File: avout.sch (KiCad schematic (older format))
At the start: 53 parts, among them CN6 AUDIO_VIDEO, M1 Modulator, Q3 2SC1815, Q81 2SC1815, Q82 2SC1815

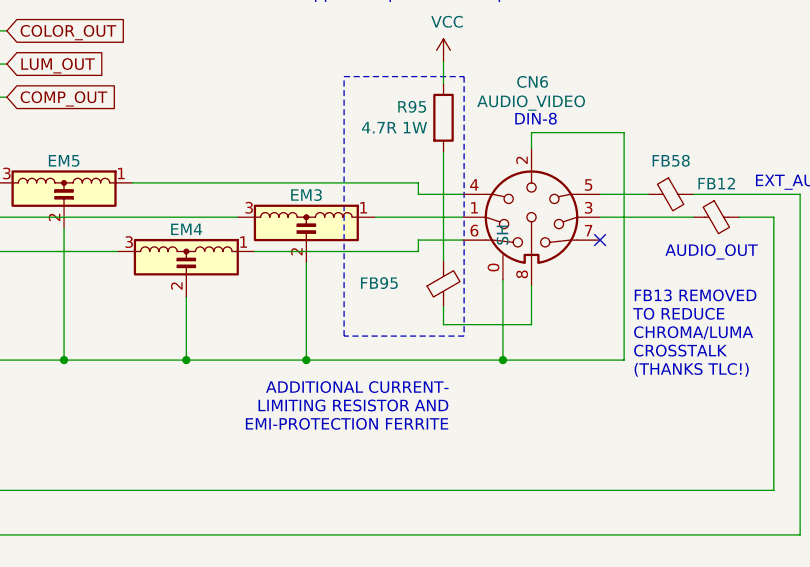
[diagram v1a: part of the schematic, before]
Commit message: Add ROM bank switcher (All-in-one ROM only)
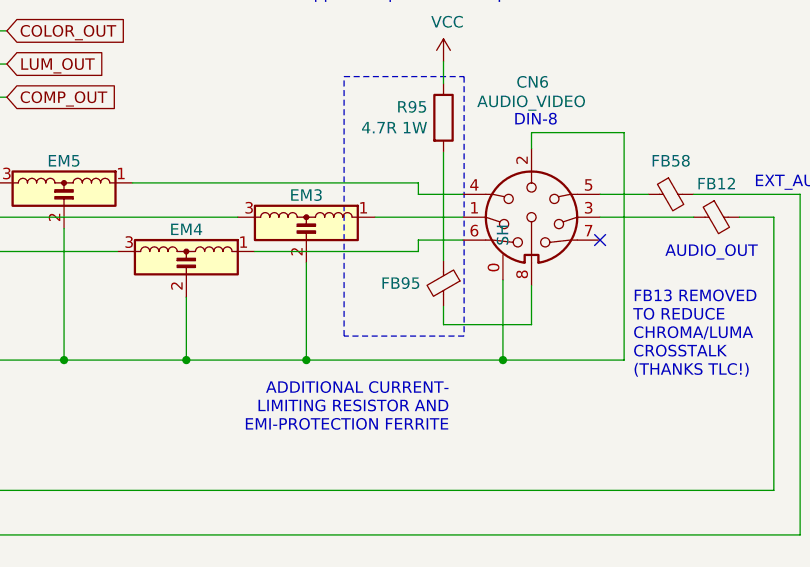
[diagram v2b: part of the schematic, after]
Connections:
- net at R95.2: now also FB95.1; no longer FB95.2
- net at CN6.8: now also FB95.2; no longer FB95.1
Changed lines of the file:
@@
 U 1 1 61E4B6DF
 P 9260 2605
-F 0 "FB95" H 9066 2605 50  0000 R CNN
+F 0 "FB95" H 9360 2605 50  0000 L CNN
 F 1 "Ferrite_Bead_Small" H 9360 2560 50  0001 L CNN
 F 2 "LittleSixteen:Ferrite" V 9190 2605 50  0001 C CNN
 F 3 "~" H 9260 2605 50  0001 C CNN
 	1    9260 2605
-	1    0    0    1
+	-1   0    0    -1
 $EndComp
 Wire Wire Line

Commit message: Rationalize BOM There should be no significant changes on both schematics on PCB, just some values and something on the silkscreen
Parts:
- removed EM3, EM4, EM5: EMI_Filter_LCL, LittleSixteen:EMI_Filter, symbol Device:EMI_Filter_LCL
- added EM3, EM4, EM5: DSS1NB32A271Q91A, LittleSixteen:EMI_Filter, symbol emi_filter_3pin:EMI_Filter_3Pin
- C11, C85: MouserPN (none) -> 810-FG28X7R1H104KNT0
- C83: value 100u/25V -> 100u/35V
- C84: MouserPN (none) -> 810-FG28C0G2A101JNT6
- FB12, FB58, FB95: value Ferrite_Bead_Small -> DSS1NB32A271Q91A; footprint LittleSixteen:Ferrite -> LittleSixteen:EMI_Filter; symbol ferrite_bead_small:Ferrite_Bead_Small -> emi_filter_3pin:EMI_Filter_3Pin
- JP81: value RV1_BYPASS -> JMP_RV1_BYPASS
- JP82: value RV2_BYPASS -> JMP_RV2_BYPASS
- L80, L81: value 10u -> FERRITE; MouserPN (none) -> 875-28C0236-0EW-10
- R95: value 4.7R 1W -> 4.7 1W
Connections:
- net COLOR_OUT: now also EM4.2
- net COMP_OUT: now also EM5.2
- net GND: now also EM3.3 (GND), EM4.3 (GND), EM5.3 (GND)
- net LUM_OUT: now also EM3.2
- net VCC: now also R95.2; no longer R95.1
- net at CN6.4: now also EM5.1
- net at CN6.1: now also EM3.1
- net at CN6.6: now also EM4.1
- net at FB95.1: now also R95.1; no longer R95.2
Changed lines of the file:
@@
 F 2 "Capacitor_THT:C_Disc_D8.0mm_W2.5mm_P5.00mm" H 1033 5430 50  0001 C CNN
 F 3 "~" H 995 5580 50  0001 C CNN
+F 4 "810-FG28X7R1H104KNT0" H 995 5580 50  0001 C CNN "MouserPN"
 	1    995  5580
 	1    0    0    -1
@@
 	1    0    0    -1
 $EndComp
-$Comp
-L Device:EMI_Filter_LCL EM5
-U 1 1 5E029075
-P 7600 2265
-F 0 "EM5" H 7600 2460 50  0000 C CNN
-F 1 "EMI_Filter_LCL" H 7600 2491 50  0001 C CNN
-F 2 "LittleSixteen:EMI_Filter" V 7600 2265 50  0001 C CNN
-F 3 "http://www.murata.com/~/media/webrenewal/support/library/catalog/products/emc/emifil/c31e.ashx?la=en-gb" V 7600 2265 50  0001 C CNN
-	1    7600 2265
-	-1   0    0    -1
-$EndComp
-$Comp
-L Device:EMI_Filter_LCL EM3
-U 1 1 5E02CB2E
-P 8660 2415
-F 0 "EM3" H 8660 2610 50  0000 C CNN
-F 1 "EMI_Filter_LCL" H 8660 2641 50  0001 C CNN
-F 2 "LittleSixteen:EMI_Filter" V 8660 2415 50  0001 C CNN
-F 3 "http://www.murata.com/~/media/webrenewal/support/library/catalog/products/emc/emifil/c31e.ashx?la=en-gb" V 8660 2415 50  0001 C CNN
-	1    8660 2415
-	-1   0    0    -1
-$EndComp
-$Comp
-L Device:EMI_Filter_LCL EM4
-U 1 1 5E02E767
-P 8135 2565
-F 0 "EM4" H 8135 2760 50  0000 C CNN
-F 1 "EMI_Filter_LCL" H 8135 2791 50  0001 C CNN
-F 2 "LittleSixteen:EMI_Filter" V 8135 2565 50  0001 C CNN
-F 3 "http://www.murata.com/~/media/webrenewal/support/library/catalog/products/emc/emifil/c31e.ashx?la=en-gb" V 8135 2565 50  0001 C CNN
-	1    8135 2565
-	-1   0    0    -1
-$EndComp
 Wire Wire Line
 	6660 2165 7210 2165
@@
 	6660 2315 7125 2315
 Wire Wire Line
-	8960 2315 9345 2315
-Wire Wire Line
-	8435 2465 9150 2465
-Wire Wire Line
-	9150 2465 9150 2415
-Wire Wire Line
 	9150 2415 9345 2415
 Wire Wire Line
@@
 Wire Wire Line
 	9150 2215 9345 2215
-Wire Wire Line
-	7900 2165 9150 2165
-Wire Wire Line
-	7600 2365 7600 2940
-Wire Wire Line
-	8135 2665 8135 2940
-Wire Wire Line
-	8135 2940 7600 2940
-Connection ~ 7600 2940
-Wire Wire Line
-	8660 2515 8660 2940
-Wire Wire Line
-	8660 2940 8135 2940
-Connection ~ 8135 2940
 Text Notes 9760 1925 2    50   ~ 0
 DIN-8
@@
 Wire Wire Line
 	10050 2940 9520 2940
-Connection ~ 8660 2940
 Wire Wire Line
 	9645 2615 9645 2785
@@
 $EndComp
 $Comp
-L ferrite_bead_small:Ferrite_Bead_Small FB12
+L emi_filter_3pin:EMI_Filter_3Pin FB12
 U 1 1 5E03F938
 P 10455 2315
 F 0 "FB12" V 10310 2315 50  0000 C CNN
-F 1 "Ferrite_Bead_Small" H 10555 2270 50  0001 L CNN
-F 2 "LittleSixteen:Ferrite" V 10385 2315 50  0001 C CNN
+F 1 "DSS1NB32A271Q91A" H 10555 2270 50  0001 L CNN
+F 2 "LittleSixteen:EMI_Filter" V 10385 2315 50  0001 C CNN
 F 3 "~" H 10455 2315 50  0001 C CNN
 	1    10455 2315
@@
 $EndComp
 $Comp
-L ferrite_bead_small:Ferrite_Bead_Small FB58
+L emi_filter_3pin:EMI_Filter_3Pin FB58
 U 1 1 5E040A9B
 P 10255 2215
 F 0 "FB58" V 10110 2215 50  0000 C CNN
-F 1 "Ferrite_Bead_Small" H 10355 2170 50  0001 L CNN
-F 2 "LittleSixteen:Ferrite" V 10185 2215 50  0001 C CNN
+F 1 "DSS1NB32A271Q91A" H 10355 2170 50  0001 L CNN
+F 2 "LittleSixteen:EMI_Filter" V 10185 2215 50  0001 C CNN
 F 3 "~" H 10255 2215 50  0001 C CNN
 	1    10255 2215
@@
 P 4805 6860
 F 0 "L81" V 4995 6860 50  0000 C CNN
-F 1 "10u" V 4904 6860 50  0000 C CNN
+F 1 "FERRITE" V 4904 6860 50  0000 C CNN
 F 2 "Inductor_THT:L_Axial_L7.0mm_D3.3mm_P12.70mm_Horizontal_Fastron_MICC" H 4805 6860 50  0001 C CNN
 F 3 "~" H 4805 6860 50  0001 C CNN
+F 4 "875-28C0236-0EW-10" H 4805 6860 50  0001 C CNN "MouserPN"
 	1    4805 6860
 	0    -1   -1   0
@@
 P 1260 5580
 F 0 "C83" H 1145 5626 50  0000 R CNN
-F 1 "100u/25V" H 1145 5535 50  0000 R CNN
+F 1 "100u/35V" H 1145 5535 50  0000 R CNN
 F 2 "Capacitor_THT:CP_Radial_D6.3mm_P2.50mm" H 1260 5580 50  0001 C CNN
 F 3 "~" H 1260 5580 50  0001 C CNN
@@
 Connection ~ 7040 2465
 Wire Wire Line
-	7040 2465 7835 2465
-Wire Wire Line
 	7125 2315 7125 1645
 Wire Wire Line
@@
 Connection ~ 7125 2315
 Wire Wire Line
-	7125 2315 8360 2315
-Wire Wire Line
 	7210 2165 7210 1790
 Wire Wire Line
 	7210 1790 7350 1790
 Connection ~ 7210 2165
-Wire Wire Line
-	7210 2165 7300 2165
 Text GLabel 7350 1790 2    50   Input ~ 0
 COMP_OUT
@@
 	9520 2590 9520 2940
 Connection ~ 9520 2940
-Wire Wire Line
-	9520 2940 8660 2940
 $Comp
 L Device:R R?
@@
 AR Path="/61BCD018/61DEF839" Ref="R?"  Part="1"
 AR Path="/5E019FCB/61DEF839" Ref="R95"  Part="1"
-F 0 "R95" H 9190 1926 50  0000 R CNN
-F 1 "4.7R 1W" H 9190 1835 50  0000 R CNN
+F 0 "R95" H 9330 1834 50  0000 L CNN
+F 1 "4.7 1W" H 9330 1925 50  0000 L CNN
 F 2 "Resistor_THT:R_Axial_DIN0414_L11.9mm_D4.5mm_P5.08mm_Vertical" V 9190 1880 50  0001 C CNN
 F 3 "~" H 9260 1880 50  0001 C CNN
 	1    9260 1880
-	1    0    0    -1
+	-1   0    0    1
 $EndComp
 Wire Wire Line
 	9260 1730 9260 1635
 $Comp
-L ferrite_bead_small:Ferrite_Bead_Small FB95
+L emi_filter_3pin:EMI_Filter_3Pin FB95
 U 1 1 61E4B6DF
 P 9260 2605
 F 0 "FB95" H 9360 2605 50  0000 L CNN
-F 1 "Ferrite_Bead_Small" H 9360 2560 50  0001 L CNN
-F 2 "LittleSixteen:Ferrite" V 9190 2605 50  0001 C CNN
+F 1 "DSS1NB32A271Q91A" H 9360 2560 50  0001 L CNN
+F 2 "LittleSixteen:EMI_Filter" V 9190 2605 50  0001 C CNN
 F 3 "~" H 9260 2605 50  0001 C CNN
 	1    9260 2605
@@
 P 3985 7345
 F 0 "L80" V 4175 7345 50  0000 C CNN
-F 1 "10u" V 4084 7345 50  0000 C CNN
+F 1 "FERRITE" V 4084 7345 50  0000 C CNN
 F 2 "Inductor_THT:L_Radial_D6.0mm_P4.00mm" H 3985 7345 50  0001 C CNN
 F 3 "~" H 3985 7345 50  0001 C CNN
+F 4 "875-28C0236-0EW-10" H 3985 7345 50  0001 C CNN "MouserPN"
 	1    3985 7345
 	0    -1   -1   0
@@
 Wire Wire Line
 	1130 5775 1260 5775
-Wire Wire Line
-	6480 2940 7600 2940
 $Comp
 L power:VCC #PWR0178
@@
 F 2 "Capacitor_THT:C_Disc_D8.0mm_W2.5mm_P5.00mm" H 3833 4555 50  0001 C CNN
 F 3 "~" H 3795 4705 50  0001 C CNN
+F 4 "810-FG28X7R1H104KNT0" H 3795 4705 50  0001 C CNN "MouserPN"
 	1    3795 4705
 	0    -1   -1   0
@@
 P 4835 5175
 F 0 "JP81" H 4835 5387 50  0000 C CNN
-F 1 "RV1_BYPASS" H 4835 5296 50  0000 C CNN
+F 1 "JMP_RV1_BYPASS" H 4835 5296 50  0000 C CNN
 F 2 "Jumper:SolderJumper-2_P1.3mm_Bridged_RoundedPad1.0x1.5mm" H 4835 5175 50  0001 C CNN
 F 3 "~" H 4835 5175 50  0001 C CNN
@@
 P 9215 5420
 F 0 "JP82" H 9215 5632 50  0000 C CNN
-F 1 "RV2_BYPASS" H 9215 5541 50  0000 C CNN
+F 1 "JMP_RV2_BYPASS" H 9215 5541 50  0000 C CNN
 F 2 "Jumper:SolderJumper-2_P1.3mm_Bridged_RoundedPad1.0x1.5mm" H 9215 5420 50  0001 C CNN
 F 3 "~" H 9215 5420 50  0001 C CNN
@@
 F 2 "Capacitor_THT:C_Disc_D8.0mm_W2.5mm_P5.00mm" H 2758 5250 50  0001 C CNN
 F 3 "~" H 2720 5400 50  0001 C CNN
+F 4 "810-FG28C0G2A101JNT6" H 2720 5400 50  0001 C CNN "MouserPN"
 	1    2720 5400
 	-1   0    0    1
@@
 Text Notes 10090 3020 0    50   ~ 0
 FB13 REMOVED\nTO REDUCE\nCHROMA/LUMA\nCROSSTALK\n(THANKS TLC!)
+Wire Wire Line
+	6480 2940 9520 2940
+Wire Wire Line
+	7210 2165 7475 2165
+Wire Wire Line
+	7675 2165 9150 2165
+$Comp
+L emi_filter_3pin:EMI_Filter_3Pin EM5
+U 1 1 67130B45
+P 7575 2165
+F 0 "EM5" V 7720 2165 50  0000 C CNN
+F 1 "DSS1NB32A271Q91A" H 7675 2120 50  0001 L CNN
+F 2 "LittleSixteen:EMI_Filter" V 7505 2165 50  0001 C CNN
+F 3 "~" H 7575 2165 50  0001 C CNN
+	1    7575 2165
+	0    1    -1   0
+$EndComp
+$Comp
+L emi_filter_3pin:EMI_Filter_3Pin EM4
+U 1 1 6714E1C3
+P 8145 2465
+F 0 "EM4" V 8000 2465 50  0000 C CNN
+F 1 "DSS1NB32A271Q91A" H 8245 2420 50  0001 L CNN
+F 2 "LittleSixteen:EMI_Filter" V 8075 2465 50  0001 C CNN
+F 3 "~" H 8145 2465 50  0001 C CNN
+	1    8145 2465
+	0    1    -1   0
+$EndComp
+Wire Wire Line
+	7040 2465 8045 2465
+$Comp
+L emi_filter_3pin:EMI_Filter_3Pin EM3
+U 1 1 6716F690
+P 8620 2315
+F 0 "EM3" V 8475 2315 50  0000 C CNN
+F 1 "DSS1NB32A271Q91A" H 8720 2270 50  0001 L CNN
+F 2 "LittleSixteen:EMI_Filter" V 8550 2315 50  0001 C CNN
+F 3 "~" H 8620 2315 50  0001 C CNN
+	1    8620 2315
+	0    1    -1   0
+$EndComp
+Wire Wire Line
+	7125 2315 8520 2315
+Wire Wire Line
+	8720 2315 9345 2315
+Wire Wire Line
+	9150 2495 8360 2495
+Wire Wire Line
+	8360 2495 8360 2465
+Wire Wire Line
+	8360 2465 8245 2465
+Wire Wire Line
+	9150 2415 9150 2495
 $EndSCHEMATC

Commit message: Rationalize capacitor footprints & BOM
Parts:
- C18, C19, C62: footprint Capacitor_THT:CP_Radial_D5.0mm_P2.50mm -> Capacitor_THT:CP_Radial_D5.0mm_P2.00mm; MouserPN (none) -> 710-860010672009
- C31: footprint Capacitor_THT:CP_Radial_D6.3mm_P2.50mm -> Capacitor_THT:CP_Radial_D5.0mm_P2.00mm; MouserPN (none) -> 710-860010672009
- JP81, JP82: MouserPN (none) -> ---
- L1: value 1.2u -> FERRITE; MouserPN (none) -> 875-28C0236-0EW-10
- L81: value FERRITE -> 10u; MouserPN 875-28C0236-0EW-10 -> 542-78F100-RC
- R11, R25: MouserPN (none) -> 603-MFR-25FBF52-100K
- R23: MouserPN (none) -> 603-MFR-25FTF52-10K
- R24, R28, R43, R8, R82: MouserPN (none) -> 603-MFR-25FBF52-1K
- R85: MouserPN (none) -> 708-RNF14FTD100R
- RV1: MouserPN (none) -> 652-3296W-1-102LF
- RV2: MouserPN (none) -> 652-3296W-1-221LF
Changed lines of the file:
@@
 P 6010 1220
 F 0 "L1" H 6062 1266 50  0000 L CNN
-F 1 "1.2u" H 6062 1175 50  0000 L CNN
+F 1 "FERRITE" H 6062 1175 50  0000 L CNN
 F 2 "Inductor_THT:L_Radial_D6.0mm_P4.00mm" H 6010 1220 50  0001 C CNN
 F 3 "~" H 6010 1220 50  0001 C CNN
+F 4 "875-28C0236-0EW-10" H 6010 1220 50  0001 C CNN "MouserPN"
 	1    6010 1220
 	1    0    0    -1
@@
 F 2 "Resistor_THT:R_Axial_DIN0207_L6.3mm_D2.5mm_P5.08mm_Vertical" V 1655 1965 50  0001 C CNN
 F 3 "~" H 1725 1965 50  0001 C CNN
+F 4 "603-MFR-25FBF52-1K" H 1725 1965 50  0001 C CNN "MouserPN"
 	1    1725 1965
 	0    -1   -1   0
@@
 F 2 "Resistor_THT:R_Axial_DIN0207_L6.3mm_D2.5mm_P5.08mm_Vertical" V 1380 2185 50  0001 C CNN
 F 3 "~" H 1450 2185 50  0001 C CNN
+F 4 "603-MFR-25FBF52-100K" H 1450 2185 50  0001 C CNN "MouserPN"
 	1    1450 2185
 	-1   0    0    1
@@
 F 0 "C18" V 1893 1965 50  0000 C CNN
 F 1 "10u/25V" V 1984 1965 50  0000 C CNN
-F 2 "Capacitor_THT:CP_Radial_D5.0mm_P2.50mm" H 2145 1965 50  0001 C CNN
+F 2 "Capacitor_THT:CP_Radial_D5.0mm_P2.00mm" H 2145 1965 50  0001 C CNN
 F 3 "~" H 2145 1965 50  0001 C CNN
+F 4 "710-860010672009" H 2145 1965 50  0001 C CNN "MouserPN"
 	1    2145 1965
 	0    1    1    0
@@
 F 2 "Resistor_THT:R_Axial_DIN0207_L6.3mm_D2.5mm_P5.08mm_Vertical" V 3385 1700 50  0001 C CNN
 F 3 "~" H 3455 1700 50  0001 C CNN
+F 4 "603-MFR-25FBF52-1K" H 3455 1700 50  0001 C CNN "MouserPN"
 	1    3455 1700
 	0    -1   -1   0
@@
 F 2 "Resistor_THT:R_Axial_DIN0207_L6.3mm_D2.5mm_P5.08mm_Vertical" V 3020 1385 50  0001 C CNN
 F 3 "~" H 3090 1385 50  0001 C CNN
+F 4 "603-MFR-25FTF52-10K" H 3090 1385 50  0001 C CNN "MouserPN"
 	1    3090 1385
 	-1   0    0    1
@@
 F 0 "C31" V 4708 2935 50  0000 C CNN
 F 1 "10u/25V" V 4799 2935 50  0000 C CNN
-F 2 "Capacitor_THT:CP_Radial_D6.3mm_P2.50mm" H 4960 2935 50  0001 C CNN
+F 2 "Capacitor_THT:CP_Radial_D5.0mm_P2.00mm" H 4960 2935 50  0001 C CNN
 F 3 "~" H 4960 2935 50  0001 C CNN
+F 4 "710-860010672009" H 4960 2935 50  0001 C CNN "MouserPN"
 	1    4960 2935
 	0    -1   1    0
@@
 F 2 "Resistor_THT:R_Axial_DIN0207_L6.3mm_D2.5mm_P5.08mm_Vertical" V 5220 3165 50  0001 C CNN
 F 3 "~" H 5290 3165 50  0001 C CNN
+F 4 "603-MFR-25FBF52-100K" H 5290 3165 50  0001 C CNN "MouserPN"
 	1    5290 3165
 	-1   0    0    1
@@
 F 2 "Resistor_THT:R_Axial_DIN0207_L6.3mm_D2.5mm_P5.08mm_Vertical" V 2060 5395 50  0001 C CNN
 F 3 "~" H 2130 5395 50  0001 C CNN
+F 4 "603-MFR-25FBF52-1K" H 2130 5395 50  0001 C CNN "MouserPN"
 	1    2130 5395
 	1    0    0    -1
@@
 F 2 "Potentiometer_THT:Potentiometer_Bourns_3296W_Vertical" H 4570 5395 50  0001 C CNN
 F 3 "~" H 4570 5395 50  0001 C CNN
+F 4 "652-3296W-1-102LF" H 4570 5395 50  0001 C CNN "MouserPN"
 	1    4570 5395
 	0    -1   -1   0
@@
 F 2 "Resistor_THT:R_Axial_DIN0207_L6.3mm_D2.5mm_P5.08mm_Vertical" V 4855 5620 50  0001 C CNN
 F 3 "~" H 4925 5620 50  0001 C CNN
+F 4 "708-RNF14FTD100R" H 4925 5620 50  0001 C CNN "MouserPN"
 	1    4925 5620
 	1    0    0    -1
@@
 F 2 "Potentiometer_THT:Potentiometer_Bourns_3296W_Vertical" H 8950 5640 50  0001 C CNN
 F 3 "~" H 8950 5640 50  0001 C CNN
+F 4 "652-3296W-1-221LF" H 8950 5640 50  0001 C CNN "MouserPN"
 	1    8950 5640
 	0    -1   -1   0
@@
 P 4805 6860
 F 0 "L81" V 4995 6860 50  0000 C CNN
-F 1 "FERRITE" V 4904 6860 50  0000 C CNN
+F 1 "10u" V 4904 6860 50  0000 C CNN
 F 2 "Inductor_THT:L_Axial_L7.0mm_D3.3mm_P12.70mm_Horizontal_Fastron_MICC" H 4805 6860 50  0001 C CNN
 F 3 "~" H 4805 6860 50  0001 C CNN
-F 4 "875-28C0236-0EW-10" H 4805 6860 50  0001 C CNN "MouserPN"
+F 4 "542-78F100-RC" H 4805 6860 50  0001 C CNN "MouserPN"
 	1    4805 6860
 	0    -1   -1   0
@@
 F 2 "Jumper:SolderJumper-2_P1.3mm_Bridged_RoundedPad1.0x1.5mm" H 4835 5175 50  0001 C CNN
 F 3 "~" H 4835 5175 50  0001 C CNN
+F 4 "---" H 4835 5175 50  0001 C CNN "MouserPN"
 	1    4835 5175
 	1    0    0    -1
@@
 F 2 "Jumper:SolderJumper-2_P1.3mm_Bridged_RoundedPad1.0x1.5mm" H 9215 5420 50  0001 C CNN
 F 3 "~" H 9215 5420 50  0001 C CNN
+F 4 "---" H 9215 5420 50  0001 C CNN "MouserPN"
 	1    9215 5420
 	1    0    0    -1
@@
 F 0 "C19" V 1893 1450 50  0000 C CNN
 F 1 "10u/25V" V 1984 1450 50  0000 C CNN
-F 2 "Capacitor_THT:CP_Radial_D5.0mm_P2.50mm" H 2145 1450 50  0001 C CNN
+F 2 "Capacitor_THT:CP_Radial_D5.0mm_P2.00mm" H 2145 1450 50  0001 C CNN
 F 3 "~" H 2145 1450 50  0001 C CNN
+F 4 "710-860010672009" H 2145 1450 50  0001 C CNN "MouserPN"
 	1    2145 1450
 	0    1    1    0
@@
 F 2 "Resistor_THT:R_Axial_DIN0207_L6.3mm_D2.5mm_P5.08mm_Vertical" V 1655 1450 50  0001 C CNN
 F 3 "~" H 1725 1450 50  0001 C CNN
+F 4 "603-MFR-25FBF52-1K" H 1725 1450 50  0001 C CNN "MouserPN"
 	1    1725 1450
 	0    -1   -1   0
@@
 F 0 "C62" V 1893 950 50  0000 C CNN
 F 1 "10u/25V" V 1984 950 50  0000 C CNN
-F 2 "Capacitor_THT:CP_Radial_D5.0mm_P2.50mm" H 2145 950 50  0001 C CNN
+F 2 "Capacitor_THT:CP_Radial_D5.0mm_P2.00mm" H 2145 950 50  0001 C CNN
 F 3 "~" H 2145 950 50  0001 C CNN
+F 4 "710-860010672009" H 2145 950 50  0001 C CNN "MouserPN"
 	1    2145 950
 	0    1    1    0
@@
 F 2 "Resistor_THT:R_Axial_DIN0207_L6.3mm_D2.5mm_P5.08mm_Vertical" V 1655 950 50  0001 C CNN
 F 3 "~" H 1725 950 50  0001 C CNN
+F 4 "603-MFR-25FBF52-1K" H 1725 950 50  0001 C CNN "MouserPN"
 	1    1725 950
 	0    -1   1    0

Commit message: Add note on some components
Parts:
- C18, C19, C31, C62: Notes (none) -> Audio cap recommended
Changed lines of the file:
@@
 F 3 "~" H 2145 1965 50  0001 C CNN
 F 4 "710-860010672009" H 2145 1965 50  0001 C CNN "MouserPN"
+F 5 "Audio cap recommended" H 2145 1965 50  0001 C CNN "Notes"
 	1    2145 1965
 	0    1    1    0
@@
 F 3 "~" H 4960 2935 50  0001 C CNN
 F 4 "710-860010672009" H 4960 2935 50  0001 C CNN "MouserPN"
+F 5 "Audio cap recommended" H 4960 2935 50  0001 C CNN "Notes"
 	1    4960 2935
 	0    -1   1    0
@@
 F 3 "~" H 2145 1450 50  0001 C CNN
 F 4 "710-860010672009" H 2145 1450 50  0001 C CNN "MouserPN"
+F 5 "Audio cap recommended" H 2145 1450 50  0001 C CNN "Notes"
 	1    2145 1450
 	0    1    1    0
@@
 F 3 "~" H 2145 950 50  0001 C CNN
 F 4 "710-860010672009" H 2145 950 50  0001 C CNN "MouserPN"
+F 5 "Audio cap recommended" H 2145 950 50  0001 C CNN "Notes"
 	1    2145 950
 	0    1    1    0

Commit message: Make C83 10uF
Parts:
- C18, C19, C31, C62: MouserPN 710-860010672009 -> (none)
- C83: value 100u/35V -> 10u/25V; footprint Capacitor_THT:CP_Radial_D6.3mm_P2.50mm -> Capacitor_THT:CP_Radial_D5.0mm_P2.00mm; MouserPN (none) -> 710-860010672009
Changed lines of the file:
@@
 F 2 "Capacitor_THT:CP_Radial_D5.0mm_P2.00mm" H 2145 1965 50  0001 C CNN
 F 3 "~" H 2145 1965 50  0001 C CNN
-F 4 "710-860010672009" H 2145 1965 50  0001 C CNN "MouserPN"
+F 4 "" H 2145 1965 50  0001 C CNN "MouserPN"
 F 5 "Audio cap recommended" H 2145 1965 50  0001 C CNN "Notes"
 	1    2145 1965
@@
 F 2 "Capacitor_THT:CP_Radial_D5.0mm_P2.00mm" H 4960 2935 50  0001 C CNN
 F 3 "~" H 4960 2935 50  0001 C CNN
-F 4 "710-860010672009" H 4960 2935 50  0001 C CNN "MouserPN"
+F 4 "" H 4960 2935 50  0001 C CNN "MouserPN"
 F 5 "Audio cap recommended" H 4960 2935 50  0001 C CNN "Notes"
 	1    4960 2935
@@
 P 1260 5580
 F 0 "C83" H 1145 5626 50  0000 R CNN
-F 1 "100u/35V" H 1145 5535 50  0000 R CNN
-F 2 "Capacitor_THT:CP_Radial_D6.3mm_P2.50mm" H 1260 5580 50  0001 C CNN
+F 1 "10u/25V" H 1145 5535 50  0000 R CNN
+F 2 "Capacitor_THT:CP_Radial_D5.0mm_P2.00mm" H 1260 5580 50  0001 C CNN
 F 3 "~" H 1260 5580 50  0001 C CNN
+F 4 "710-860010672009" H 1260 5580 50  0001 C CNN "MouserPN"
 	1    1260 5580
 	-1   0    0    -1
@@
 F 2 "Capacitor_THT:CP_Radial_D5.0mm_P2.00mm" H 2145 1450 50  0001 C CNN
 F 3 "~" H 2145 1450 50  0001 C CNN
-F 4 "710-860010672009" H 2145 1450 50  0001 C CNN "MouserPN"
+F 4 "" H 2145 1450 50  0001 C CNN "MouserPN"
 F 5 "Audio cap recommended" H 2145 1450 50  0001 C CNN "Notes"
 	1    2145 1450
@@
 F 2 "Capacitor_THT:CP_Radial_D5.0mm_P2.00mm" H 2145 950 50  0001 C CNN
 F 3 "~" H 2145 950 50  0001 C CNN
-F 4 "710-860010672009" H 2145 950 50  0001 C CNN "MouserPN"
+F 4 "" H 2145 950 50  0001 C CNN "MouserPN"
 F 5 "Audio cap recommended" H 2145 950 50  0001 C CNN "Notes"
 	1    2145 950
